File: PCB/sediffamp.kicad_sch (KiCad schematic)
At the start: 19 parts, among them U13 OPA1622

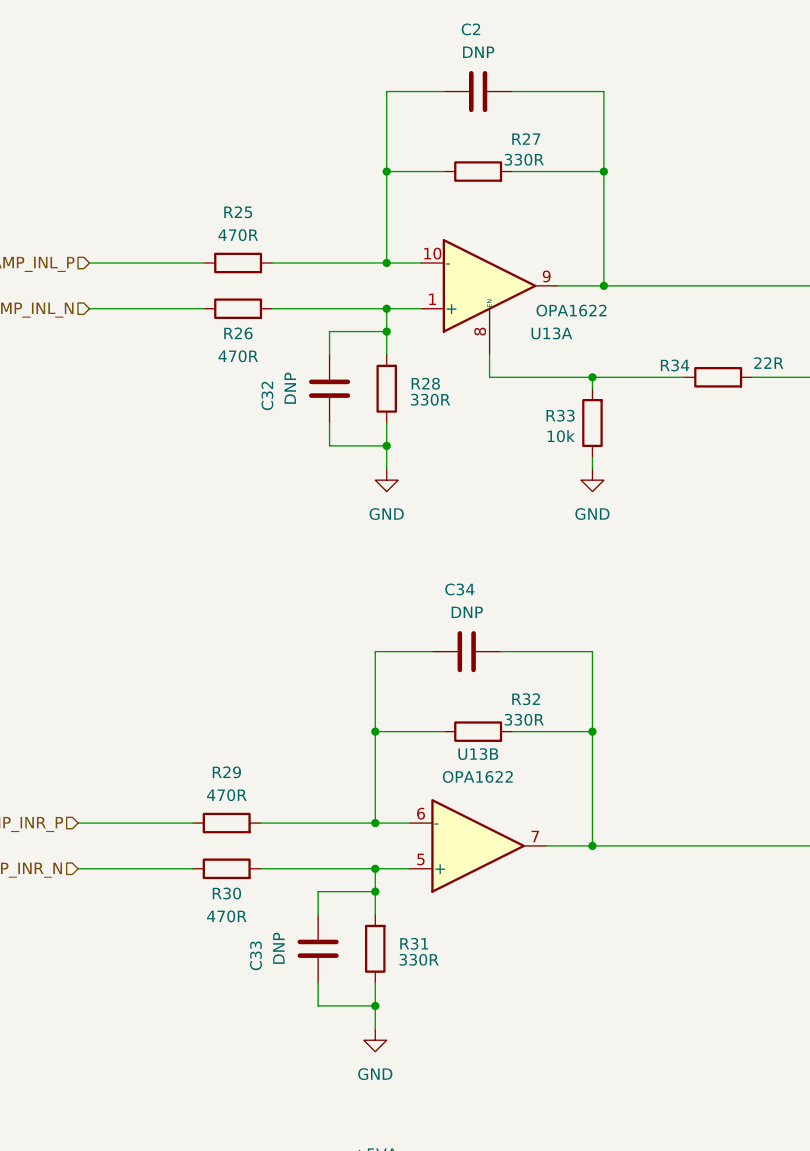
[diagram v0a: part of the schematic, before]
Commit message: Optimized designator positions and DNP for capacitors in OPA1622
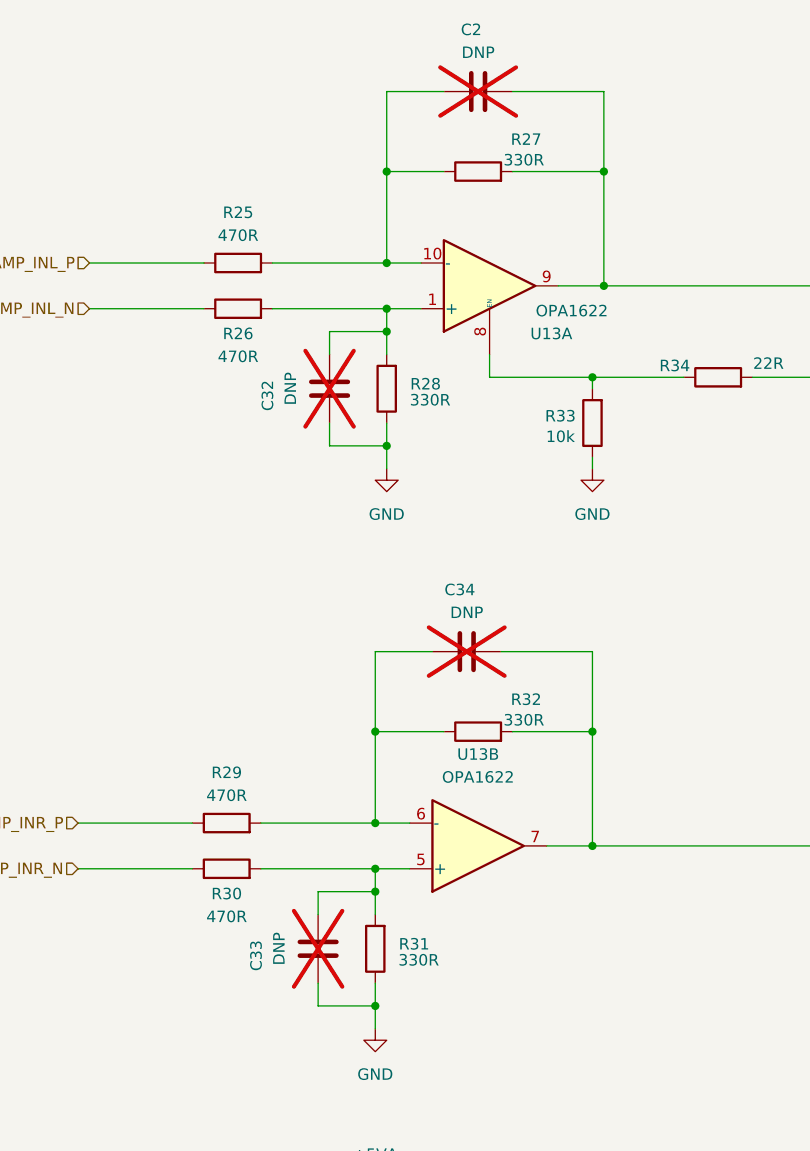
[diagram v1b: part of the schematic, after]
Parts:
- C2, C32, C33, C34: now not fitted
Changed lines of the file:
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@@
 		(in_bom yes)
 		(on_board yes)
-		(dnp no)
+		(dnp yes)
 		(property "Reference" "C34"
 			(at 136.398 87.122 90)
@@
 		(in_bom yes)
 		(on_board yes)
-		(dnp no)
+		(dnp yes)
 		(property "Reference" "C32"
 			(at 115.062 65.532 90)
@@
 		(in_bom yes)
 		(on_board yes)
-		(dnp no)
+		(dnp yes)
 		(property "Reference" "C33"
 			(at 113.792 127.762 90)
@@
 		(in_bom yes)
 		(on_board yes)
-		(dnp no)
+		(dnp yes)
 		(property "Reference" "C2"
 			(at 137.668 24.892 90)

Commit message: Redone placement and layout of OPA1622. Still finishing touches
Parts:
- removed C27, C28: 1uF, Capacitor_SMD:C_0603_1608Metric_Pad1.08x0.95mm_HandSolder, symbol Device:C
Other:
- moved on the sheet: C25, C26, U13C

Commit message: Changed the BOM field for JLCPCB to the original name instead of LCSC
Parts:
- C25, C26: JLCPCB Part # (none) -> C1525; LCSC Part # C1525 -> (none)
- R25, R26, R29, R30: JLCPCB Part # (none) -> C445590; LCSC Part # C445590 -> (none)
- R27, R28, R31, R32: JLCPCB Part # (none) -> C186314; LCSC Part # C186314 -> (none)
- R33: JLCPCB Part # (none) -> C25744; LCSC Part # C25744 -> (none)
- R34: JLCPCB Part # (none) -> C25092; LCSC Part # C25092 -> (none)
- U13: JLCPCB Part # (none) -> C2876559; LCSC Part # C2876559 -> (none)
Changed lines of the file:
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@@
 			)
 		)
-		(property "LCSC Part #" "C25744"
+		(property "JLCPCB Part #" "C25744"
 			(at 151.13 68.58 0)
 			(effects
@@
 			)
 		)
-		(property "LCSC Part #" "C2876559"
+		(property "JLCPCB Part #" "C2876559"
 			(at 140.97 166.37 0)
 			(effects
@@
 			)
 		)
-		(property "LCSC Part #" "C2876559"
+		(property "JLCPCB Part #" "C2876559"
 			(at 138.43 115.57 0)
 			(effects
@@
 			)
 		)
-		(property "LCSC Part #" "C2876559"
+		(property "JLCPCB Part #" "C2876559"
 			(at 139.7 53.34 0)
 			(effects
@@
 			)
 		)
-		(property "LCSC Part #" "C445590"
+		(property "JLCPCB Part #" "C445590"
 			(at 111.76 50.8 0)
 			(effects
@@
 			)
 		)
-		(property "LCSC Part #" "C445590"
+		(property "JLCPCB Part #" "C445590"
 			(at 110.49 113.03 0)
 			(effects
@@
 			)
 		)
-		(property "LCSC Part #" "C186314"
+		(property "JLCPCB Part #" "C186314"
 			(at 127 127 0)
 			(effects
@@
 			)
 		)
-		(property "LCSC Part #" "C445590"
+		(property "JLCPCB Part #" "C445590"
 			(at 110.49 118.11 0)
 			(effects
@@
 			)
 		)
-		(property "LCSC Part #" "C186314"
+		(property "JLCPCB Part #" "C186314"
 			(at 138.43 102.87 0)
 			(effects
@@
 			)
 		)
-		(property "LCSC Part #" "C25092"
+		(property "JLCPCB Part #" "C25092"
 			(at 165.1 63.5 0)
 			(effects
@@
 			)
 		)
-		(property "LCSC Part #" "C445590"
+		(property "JLCPCB Part #" "C445590"
 			(at 111.76 55.88 0)
 			(effects
@@
 			)
 		)
-		(property "LCSC Part #" ""
-			(at 137.16 93.98 0)
-			(effects
-				(font
-					(size 1.27 1.27)
-				)
-				(hide yes)
-			)
-		)
 		(pin "2"
 		)
@@
 			)
 		)
-		(property "LCSC Part #" ""
-			(at 121.92 64.77 0)
-			(effects
-				(font
-					(size 1.27 1.27)
-				)
-				(hide yes)
-			)
-		)
 		(pin "2"
 		)
@@
 			)
 		)
-		(property "LCSC Part #" "C186314"
+		(property "JLCPCB Part #" "C186314"
 			(at 138.43 40.64 0)
 			(effects
@@
 			)
 		)
-		(property "LCSC Part #" "C1525"
+		(property "JLCPCB Part #" "C1525"
 			(at 116.84 162.56 0)
 			(effects
@@
 			)
 		)
-		(property "LCSC Part #" "C186314"
+		(property "JLCPCB Part #" "C186314"
 			(at 128.27 64.77 0)
 			(effects
@@
 			)
 		)
-		(property "LCSC Part #" "C1525"
+		(property "JLCPCB Part #" "C1525"
 			(at 116.84 175.26 0)
 			(effects
@@
 			)
 		)
-		(property "LCSC Part #" ""
-			(at 120.65 127 0)
-			(effects
-				(font
-					(size 1.27 1.27)
-				)
-				(hide yes)
-			)
-		)
 		(pin "2"
 		)
@@
 			(at 138.43 31.75 0)
 			(effects
-				(font
-					(size 1.27 1.27)
-				)
-				(hide yes)
-			)
-		)
-		(property "LCSC Part #" ""
-			(at 138.43 31.75 0)
-			(effects

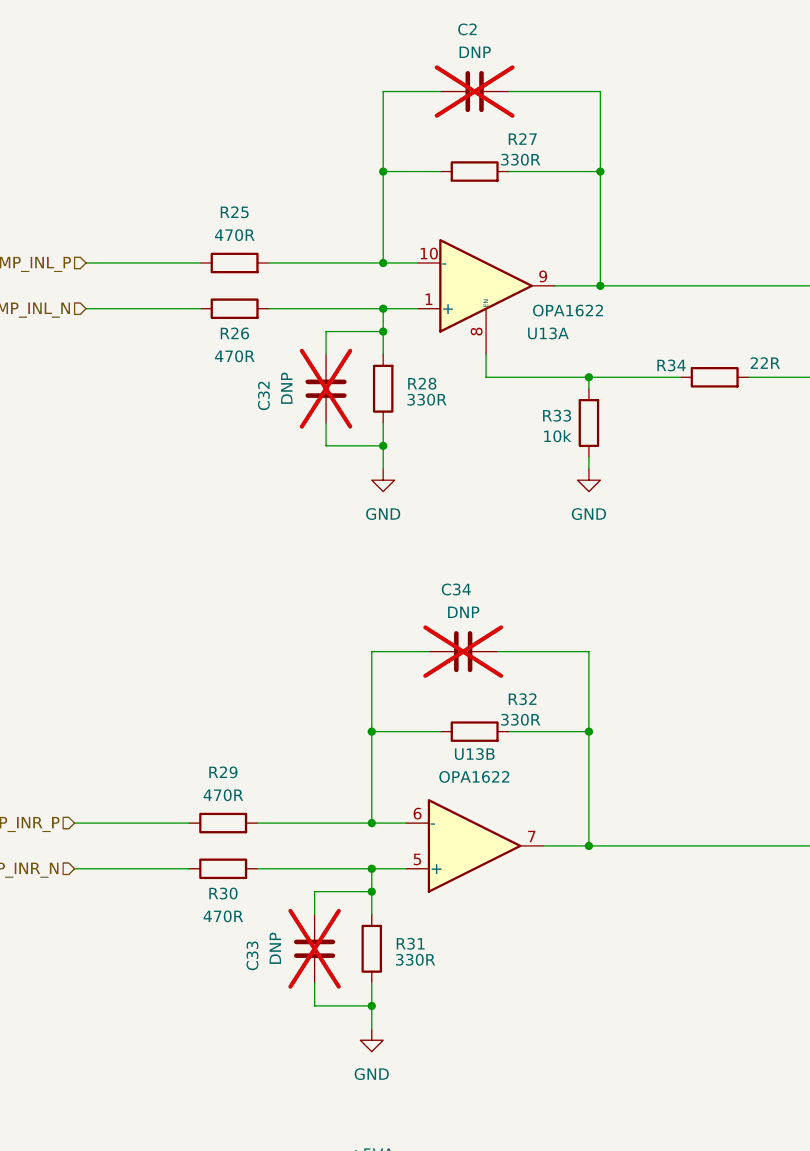
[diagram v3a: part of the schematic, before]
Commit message: Changed single ended connector for gold plated part and changed resistor and capacitor values of opa1622 amp for improved power on high impedance headphones
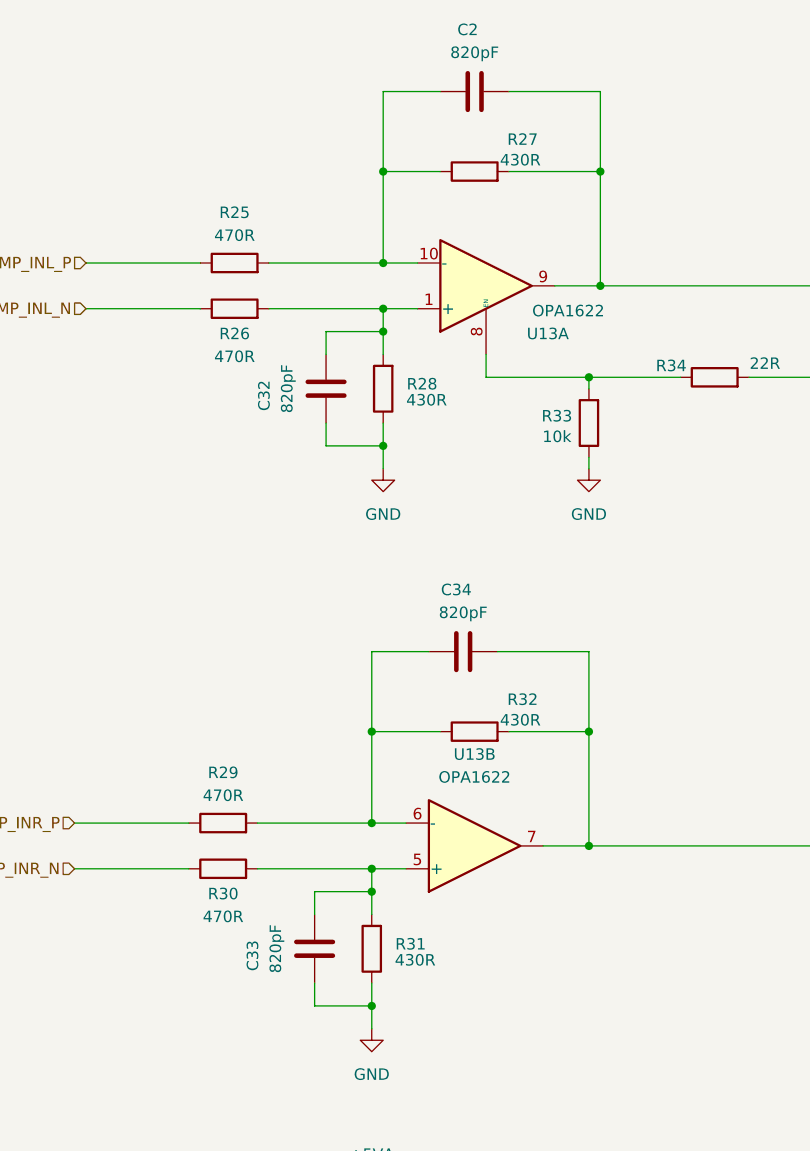
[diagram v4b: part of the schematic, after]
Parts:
- C2, C32, C33, C34: value DNP -> 820pF; JLCPCB Part # (none) -> C99081; now fitted
- R27, R28, R31, R32: value 330R -> 430R; JLCPCB Part # C186314 -> C186317
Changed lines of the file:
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@@
 			)
 		)
-		(property "Value" "330R"
+		(property "Value" "430R"
 			(at 131.826 128.27 0)
 			(effects
@@
 			)
 		)
-		(property "JLCPCB Part #" "C186314"
+		(property "JLCPCB Part #" "C186317"
 			(at 127 127 0)
 			(effects
@@
 			)
 		)
-		(property "Value" "330R"
+		(property "Value" "430R"
 			(at 143.51 101.6 90)
 			(effects
@@
 			)
 		)
-		(property "JLCPCB Part #" "C186314"
+		(property "JLCPCB Part #" "C186317"
 			(at 138.43 102.87 0)
 			(effects
@@
 		(in_bom yes)
 		(on_board yes)
-		(dnp yes)
+		(dnp no)
 		(property "Reference" "C34"
 			(at 136.398 87.122 90)
@@
 			)
 		)
-		(property "Value" "DNP"
+		(property "Value" "820pF"
 			(at 137.16 89.662 90)
 			(effects
@@
 			)
 		)
+		(property "JLCPCB Part #" "C99081"
+			(at 137.16 93.98 0)
+			(effects
+				(font
+					(size 1.27 1.27)
+				)
+				(hide yes)
+			)
+		)
 		(pin "2"
 		)
@@
 		(in_bom yes)
 		(on_board yes)
-		(dnp yes)
+		(dnp no)
 		(property "Reference" "C32"
 			(at 115.062 65.532 90)
@@
 			)
 		)
-		(property "Value" "DNP"
+		(property "Value" "820pF"
 			(at 117.602 64.77 90)
 			(effects
@@
 			)
 		)
+		(property "JLCPCB Part #" "C99081"
+			(at 121.92 64.77 0)
+			(effects
+				(font
+					(size 1.27 1.27)
+				)
+				(hide yes)
+			)
+		)
 		(pin "2"
 		)
@@
 			)
 		)
-		(property "Value" "330R"
+		(property "Value" "430R"
 			(at 143.51 39.37 90)
 			(effects
@@
 			)
 		)
-		(property "JLCPCB Part #" "C186314"
+		(property "JLCPCB Part #" "C186317"
 			(at 138.43 40.64 0)
 			(effects
@@
 			)
 		)
-		(property "Value" "330R"
+		(property "Value" "430R"
 			(at 133.096 66.04 0)
 			(effects
@@
 			)
 		)
-		(property "JLCPCB Part #" "C186314"
+		(property "JLCPCB Part #" "C186317"
 			(at 128.27 64.77 0)
 			(effects
@@
 		(in_bom yes)
 		(on_board yes)
-		(dnp yes)
+		(dnp no)
 		(property "Reference" "C33"
 			(at 113.792 127.762 90)
@@
 			)
 		)
-		(property "Value" "DNP"
+		(property "Value" "820pF"
 			(at 116.332 127 90)
 			(effects
@@
 			)
 		)
+		(property "JLCPCB Part #" "C99081"
+			(at 120.65 127 0)
+			(effects
+				(font
+					(size 1.27 1.27)
+				)
+				(hide yes)
+			)
+		)
 		(pin "2"
 		)
@@
 		(in_bom yes)
 		(on_board yes)
-		(dnp yes)
+		(dnp no)
 		(property "Reference" "C2"
 			(at 137.668 24.892 90)
@@
 			)
 		)
-		(property "Value" "DNP"
+		(property "Value" "820pF"
 			(at 138.43 27.432 90)
 			(effects
@@
 			(at 138.43 31.75 0)
 			(effects
+				(font
+					(size 1.27 1.27)
+				)
+				(hide yes)
+			)
+		)
+		(property "JLCPCB Part #" "C99081"
+			(at 138.43 31.75 0)
+			(effects
